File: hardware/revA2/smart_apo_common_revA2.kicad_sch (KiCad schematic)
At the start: 43 parts, among them J1 BATTERY, J2 POGO_DEBUG_CHARGE, J3 FULL_BRIDGE_6WIRE, Q1 2N7002, SW1 SMT_REED_NO, U1 STM32G031F8P6, U2 LSM6DSOTR, U3 LPS28DFWTR, U4 NAU7802SGI, U5 W25Q256JVEIQ, U6 MCP73831T-2ACI/OT, U7 TPS7A0233PDBVR, Y1 32.768kHz_12.5pF

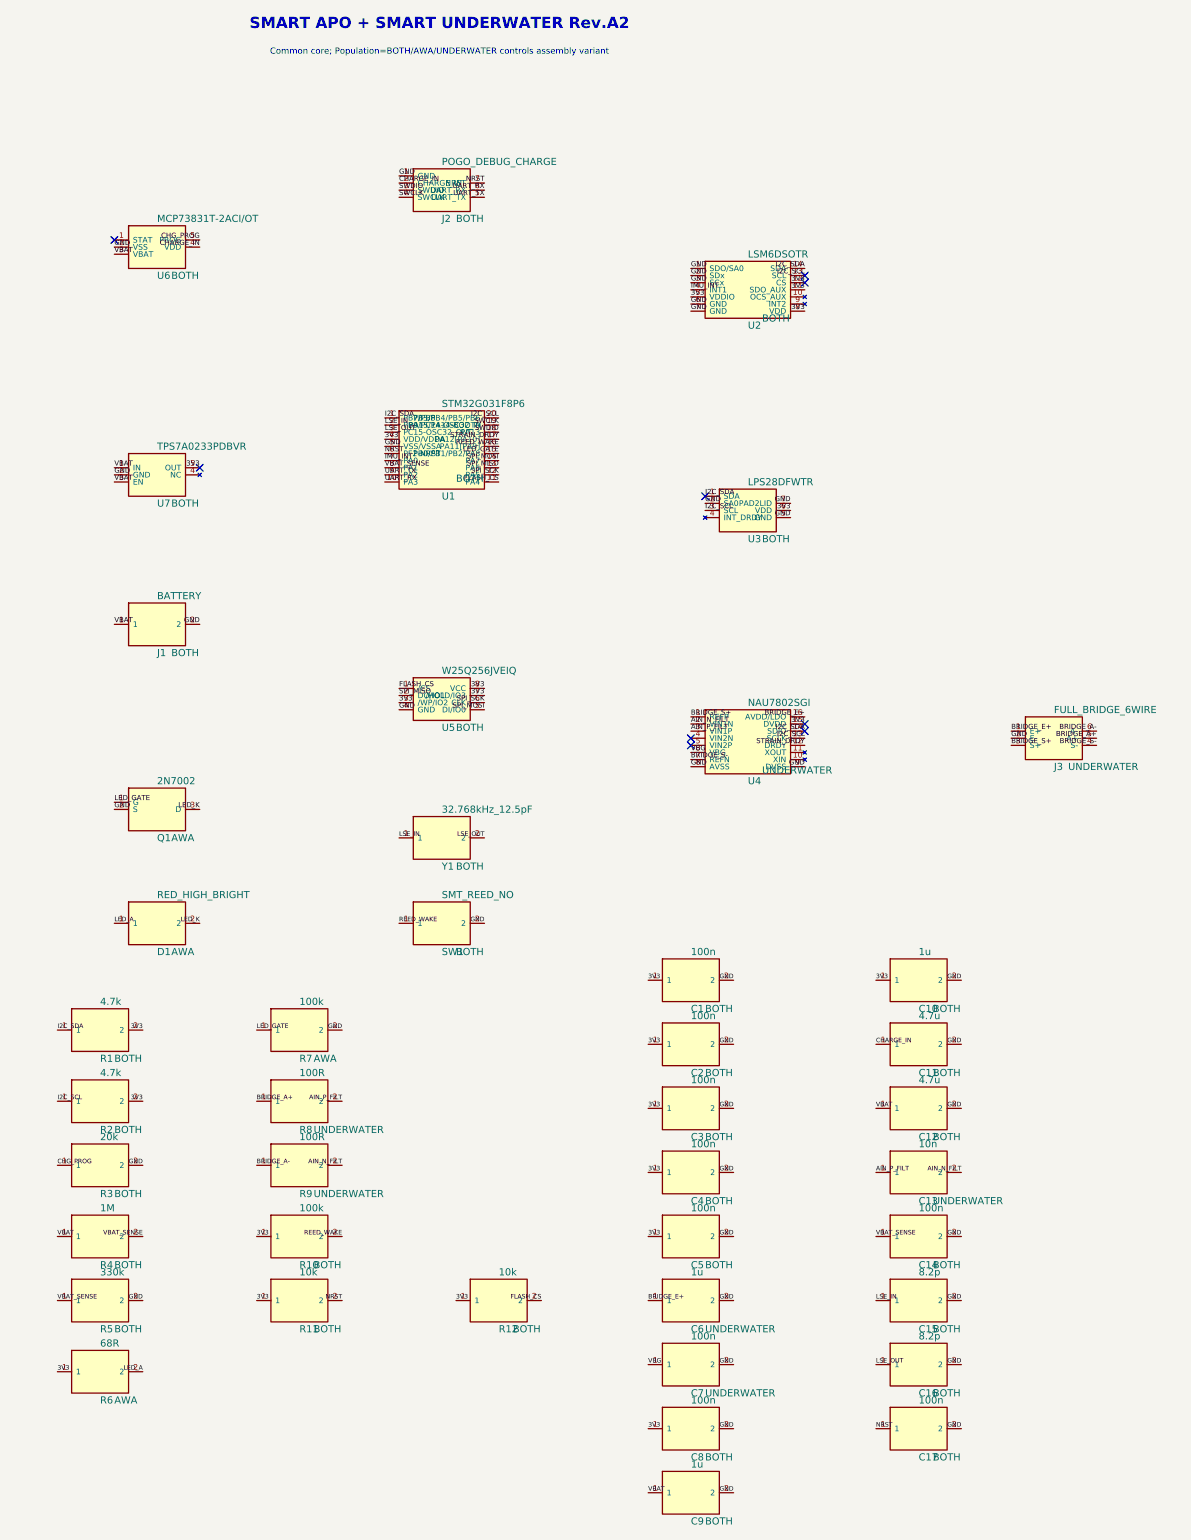
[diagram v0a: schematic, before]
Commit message: Preserve Rev.A2 engineering state for public collaboration
Capture the reviewed KiCad candidate, firmware and host tooling, and current handoff documents. Exclude transient local validation snapshots and build products from the public repository.

Constraint: Fabrication release remains blocked by assembly, sourcing, and physical verification gates

Confidence: medium

Scope-risk: broad

Directive: Treat UART voyage-header changes as work in progress until end-to-end tests cover them

Tested: 34 host tests, 8 MCU model tests, 17 tool tests, Rev.A2 structural validation, staged diff check

Not-tested: final ARM ELF, board bring-up, physical tests, new UART voyage-header end-to-end behavior
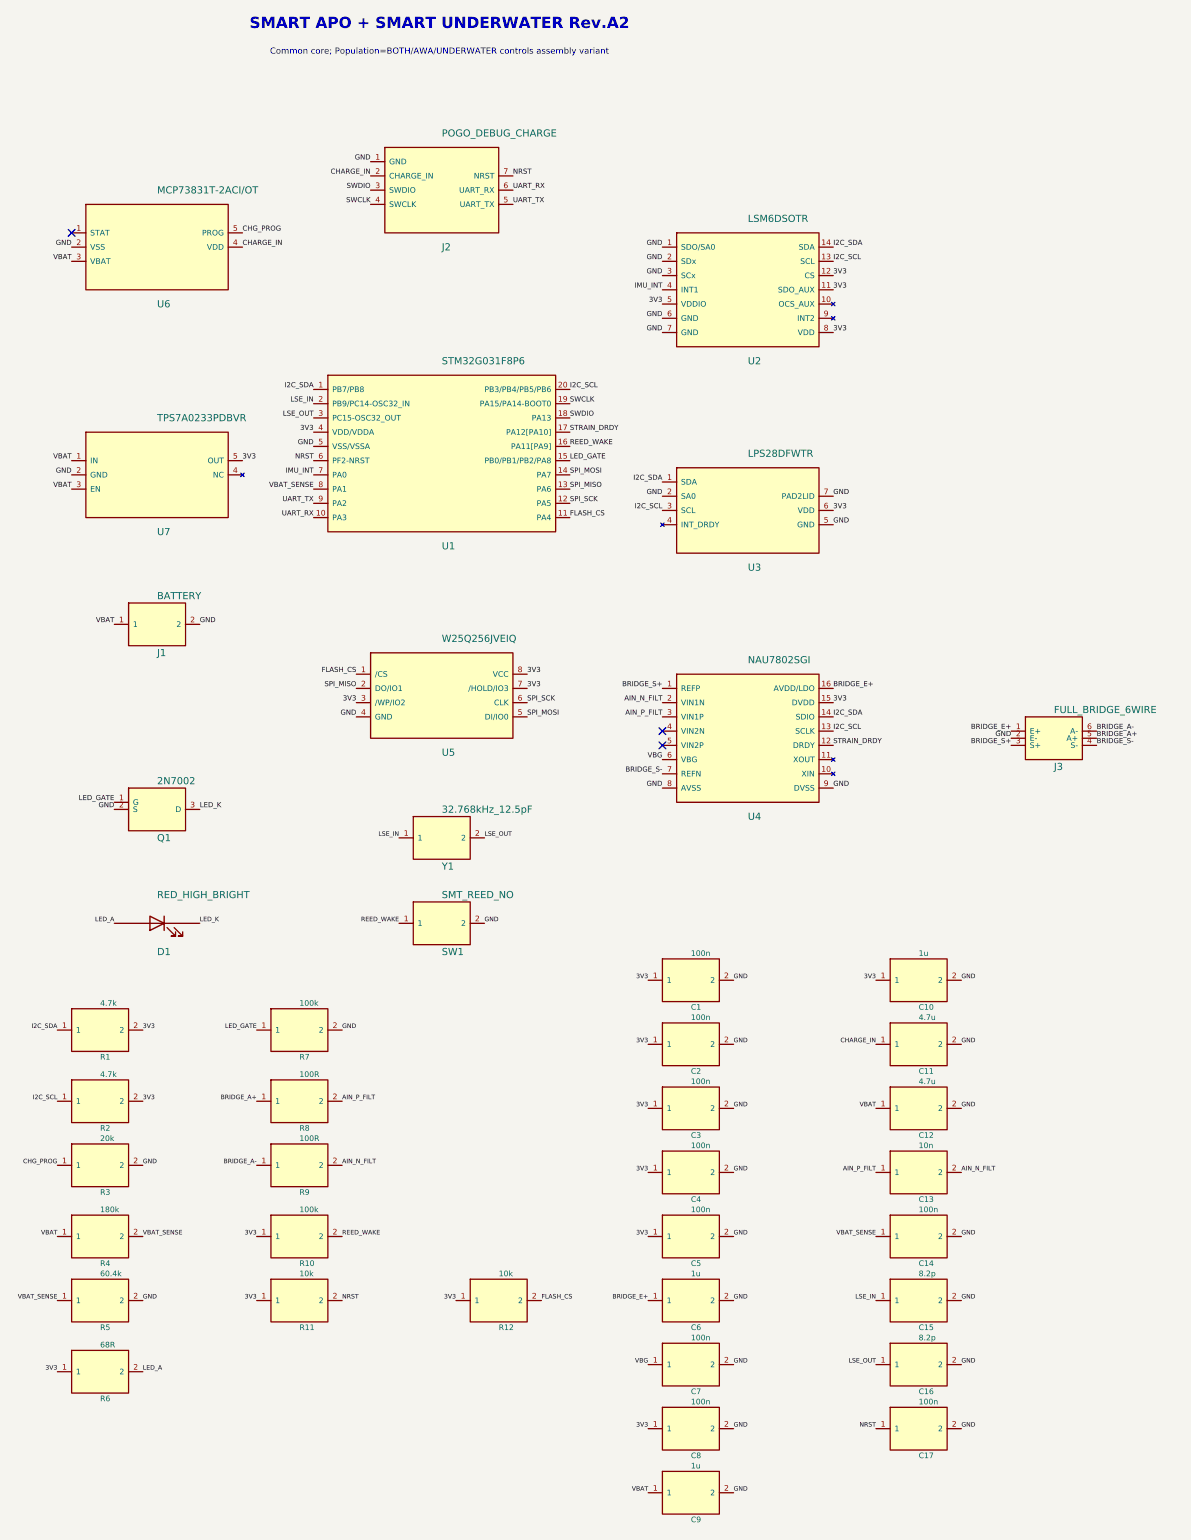
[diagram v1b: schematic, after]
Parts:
- D1: footprint LED_SMD:LED_0805_2012Metric -> SmartApoRevA2:LED_0805_2012Metric_RevA2_K1; symbol SmartApoRevA2:PASSIVE2 -> SmartApoRevA2:LED_AK_REVA2
- R4: value 1M -> 180k
- R5: value 330k -> 60.4k
- SW1: footprint Button_Switch_SMD:SW_SPST_REED_CT05-XXXX-G1 -> SmartApoRevA2:REED_CT05_COMPACT
- U1: footprint Package_SO:TSSOP-20_4.4x6.5mm_P0.65mm -> SmartApoRevA2:TSSOP-20_4.4x6.5mm_P0.65mm_RevA2_Pin1
- U2: footprint Package_LGA:LGA-14_3x2.5mm_P0.5mm_LayoutBorder3x4y -> SmartApoRevA2:LGA-14_3x2.5mm_P0.5mm_LSM6DSO
- U5: footprint Package_DFN_QFN:WDFN-8-1EP_8x6mm_P1.27mm_EP6x4.8mm -> SmartApoRevA2:WSON-8_W25Q256JV_8x6mm_AN0000009
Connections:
- net LED_A: now also D1.2 (A); no longer D1.1
- net LED_K: now also D1.1 (K); no longer D1.2
- no-connect marks 9 -> 3
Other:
- moved on the sheet: U1, U5
